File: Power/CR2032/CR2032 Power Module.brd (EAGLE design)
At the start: 25.4 x 25.4 mm, 3 parts

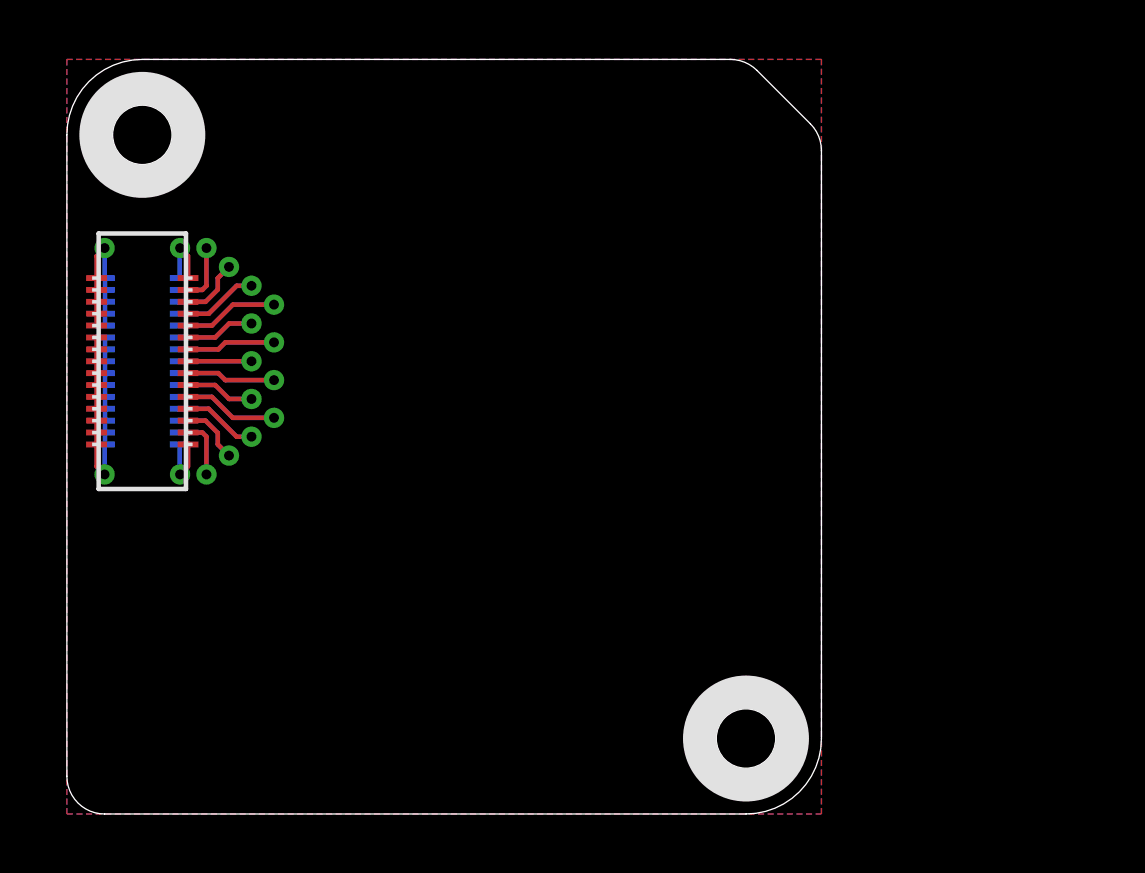
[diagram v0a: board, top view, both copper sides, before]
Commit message: Created CR2032 Power Module project.
Signed-off-by: Cruz Monrreal II <Cruz.Monrreal@gmail.com>
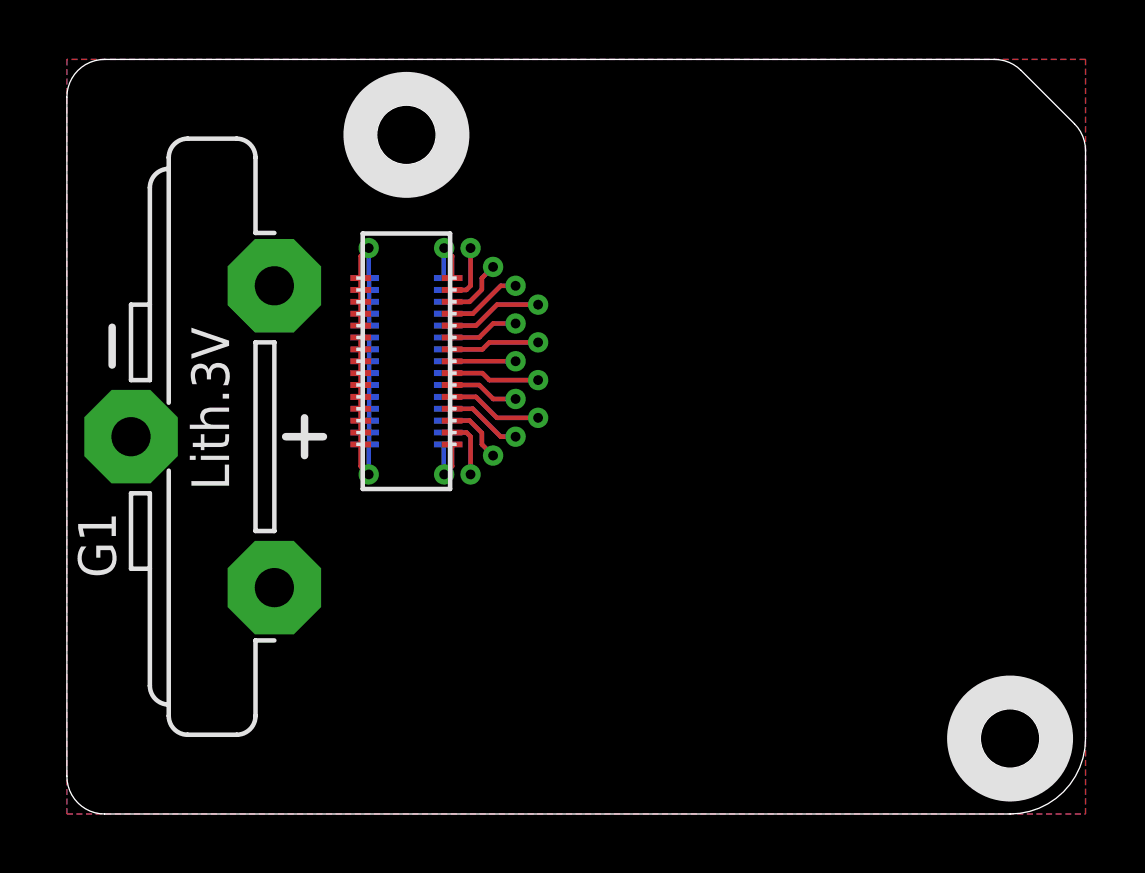
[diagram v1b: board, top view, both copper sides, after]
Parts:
- added G1: CR2032V, battery:CR2032V
- moved U$3 8.89 mm to (31.8, 2.54)
- moved U$4 8.89 mm to (11.4, 22.9)
- moved U$8 8.89 mm to (8.89, 0.00)
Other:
- board size 25.4 x 25.4 mm -> 34.3 x 25.4 mm
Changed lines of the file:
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@@
 <board>
 <plain>
-<wire x1="0" y1="22.86" x2="0" y2="1.27" width="0" layer="20"/>
+<wire x1="31.22395" y1="25.4" x2="1.27" y2="25.4" width="0" layer="20"/>
+<wire x1="1.27" y1="25.4" x2="0" y2="24.13" width="0" layer="20" curve="90"/>
+<wire x1="0" y1="24.13" x2="0" y2="1.27" width="0" layer="20"/>
 <wire x1="0" y1="1.27" x2="1.27" y2="0" width="0" layer="20" curve="90"/>
-<wire x1="1.27" y1="0" x2="22.86" y2="0" width="0" layer="20"/>
-<wire x1="22.86" y1="0" x2="25.4" y2="2.54" width="0" layer="20" curve="90"/>
-<wire x1="25.4" y1="2.54" x2="25.4" y2="22.33395" width="0" layer="20"/>
-<wire x1="25.4" y1="22.33395" x2="25.028025" y2="23.231975" width="0" layer="20" curve="45"/>
-<wire x1="25.028025" y1="23.231975" x2="23.231975" y2="25.028025" width="0" layer="20"/>
-<wire x1="23.231975" y1="25.028025" x2="22.33395" y2="25.4" width="0" layer="20" curve="45"/>
-<wire x1="22.33395" y1="25.4" x2="2.54" y2="25.4" width="0" layer="20"/>
-<wire x1="2.54" y1="25.4" x2="0" y2="22.86" width="0" layer="20" curve="90"/>
+<wire x1="1.27" y1="0" x2="31.75" y2="0" width="0" layer="20"/>
+<wire x1="31.75" y1="0" x2="34.29" y2="2.54" width="0" layer="20" curve="90"/>
+<wire x1="34.29" y1="2.54" x2="34.29" y2="22.33395" width="0" layer="20"/>
+<wire x1="34.29" y1="22.33395" x2="33.918025" y2="23.231975" width="0" layer="20" curve="45"/>
+<wire x1="33.918025" y1="23.231975" x2="32.121975" y2="25.028025" width="0" layer="20"/>
+<wire x1="32.121975" y1="25.028025" x2="31.22395" y2="25.4" width="0" layer="20" curve="45"/>
 </plain>
 <attributes>
@@
 </autorouter>
 <elements>
-<element name="U$4" library=".screw_holes" package="2MM" value="HOLE.2MM" x="2.54" y="22.86" rot="R90"/>
-<element name="U$3" library=".screw_holes" package="2MM" value="HOLE.2MM" x="22.86" y="2.54" rot="R90"/>
-<element name="U$8" library="thinkmaketest" package="ROOT1.BOTH" value="ROOT1.BOTH" x="0" y="0"/>
+<element name="U$4" library=".screw_holes" package="2MM" value="HOLE.2MM" x="11.43" y="22.86" rot="R90"/>
+<element name="U$3" library=".screw_holes" package="2MM" value="HOLE.2MM" x="31.75" y="2.54" rot="R90"/>
+<element name="U$8" library="thinkmaketest" package="ROOT1.BOTH" value="ROOT1.BOTH" x="8.89" y="0"/>
+<element name="G1" library="battery" package="CR2032V" value="CR2032V" x="4.445" y="12.7" rot="R180"/>
 </elements>
 <signals>
@@
 <polygon width="0.2032" layer="16">
 <vertex x="0" y="0"/>
-<vertex x="25.4" y="0"/>
-<vertex x="25.4" y="25.4"/>
+<vertex x="34.29" y="0"/>
+<vertex x="34.29" y="25.4"/>
 <vertex x="0" y="25.4"/>
 </polygon>
 <polygon width="0.2032" layer="1">
 <vertex x="0" y="0"/>
-<vertex x="25.4" y="0"/>
-<vertex x="25.4" y="25.4"/>
+<vertex x="34.29" y="0"/>
+<vertex x="34.29" y="25.4"/>
 <vertex x="0" y="25.4"/>
 </polygon>
